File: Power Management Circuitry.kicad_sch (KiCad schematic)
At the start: 24 parts, among them J1 Barrel_Jack_Switch, Q1 IRF7309IPBF, SW2 SW_SPST, U2 AMS1117-3.3, U3 AMS1117-5.0, U4 LM358, U5 LM358

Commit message: Update Power Management Circuitry.kicad_sch
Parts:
- removed U4, U5: LM358, Package_SO:SO-8_3.9x4.9mm_P1.27mm, symbol Amplifier_Operational:LM358
- added R3: 10 kΩ, Resistor_SMD:R_1206_3216Metric_Pad1.30x1.75mm_HandSolder, symbol Device:R
- added U4: LM324, symbol Amplifier_Operational:LM324
- added U5: LM339, symbol Comparator:LM339
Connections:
- net +3V3: now also U5.4 (-)
- net +5V_{OCP}: now also R3.2, U5.3 (V+)
- net +V_{In}: now also U4.4 (V+)
- net -V_{In}: now also U4.11 (V-), U5.12 (V-)
- net at RV3.2: now also U4.10 (+)
- net at Q1.4 (G): now also R3.1, U5.2
- net at R3.2, R4.1: now also U4.6 (-)
- net at R4.2: now also U4.7, U4.9 (-)
- net at R3.1, R4.2: now also U5.5 (+)
- net at Q1.2 (G): now also U4.8
- net at RV2.2: now also U4.3 (+)
- net at RV1.2: now also U4.2 (-)
- net at RV1.3: now also U4.1, U4.5 (+)

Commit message: Schematic Revision C2
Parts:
- removed Q1: IRF7309IPBF, Package_SO:SOIC-8_3.9x4.9mm_P1.27mm, symbol Transistor_FET:IRF7309IPBF
- added Q1: AO3401A, Package_TO_SOT_SMD:SOT-23_Handsoldering, symbol Transistor_FET:AO3401A
- added Q2: SI2302, Package_TO_SOT_SMD:SOT-23_Handsoldering, symbol M's Library:SI2302
- D1: Local Seller https://microohm-eg.com/product/blue-led-5mm/ -> https://makerselectronics.com/product/blue-led-5mm-transpar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
- F1: footprint Fuse:Fuseholder_Clip-5x20mm_Littelfuse_520_Inline_P20.50x5.80mm_D1.30mm_Horizontal -> Fuse:Fuseholder_Cylinder-5x20mm_Schurter_0031_8201_Horizontal_Open; Local Seller https://makerselectronics.com/product/fuse-holder-on-pcb-fo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 -> https://makerselectronics.com/product/fuse-holder-5mm-x-20m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
- R2: Local Seller https://makerselectronics.com/product/chip-resistor-smd-330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 -> 0.22
- U4: footprint (none) -> Package_SO:SO-14_3.9x8.65mm_P1.27mm; Local Seller (none) -> https://makerselectronics.com/product/lm324-sop-14-operatio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
- U5: footprint (none) -> Package_SO:SOIC-14_3.9x8.7mm_P1.27mm; Local Seller (none) -> https://makerselectronics.com/product/lm339d-5mv-0-25ua-4-s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
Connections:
- net +5V: now also Q1.2 (S)
- net -V_{In}: now also Q2.2 (S)
- net GND: now also Q2.3 (D)
- net VBUS: now also Q1.3 (D)
- net at R3.1, U5.2: now also Q1.1 (G)
- net at U4.8: now also Q2.1 (G)
- no-connect marks 0 -> 2
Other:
- added sheet Unplaced Units (Unplaced Units.kicad_sch)

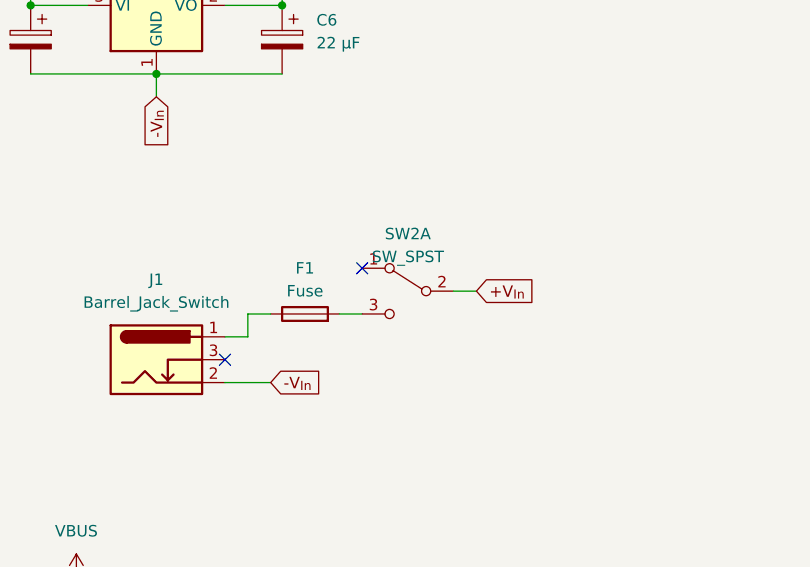
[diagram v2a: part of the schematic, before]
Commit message: Finished recreating the schematic
Created new footprints for DC Barrel Jack and Fuse Holder (3d models still require adjustment and finalize shunt resistance value and footprint)
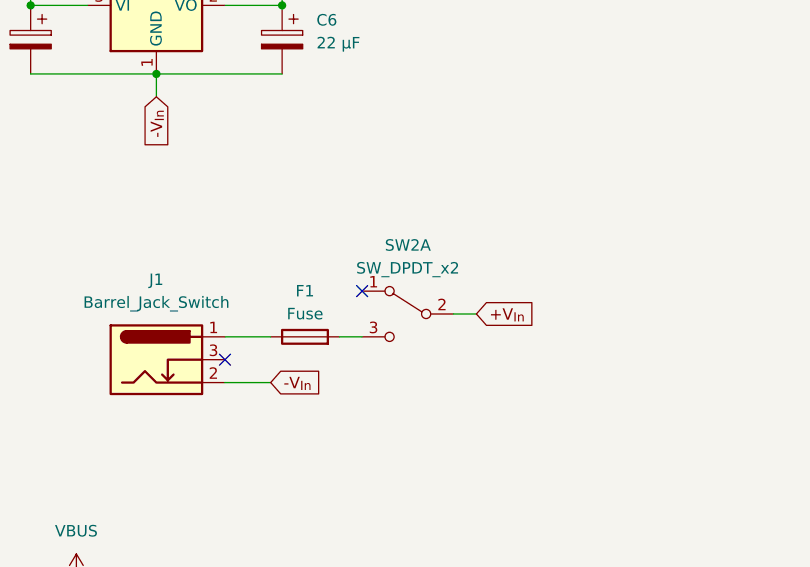
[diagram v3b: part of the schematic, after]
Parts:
- F1: footprint Fuse:Fuseholder_Cylinder-5x20mm_Schurter_0031_8201_Horizontal_Open -> M's Library:Fuseholder_with_Cover_5x20mm_Horizontal
- J1: footprint Connector_BarrelJack:BarrelJack_Horizontal -> M's Library:BarrelJack_Horizontal
- SW2: value SW_SPST -> SW_DPDT_x2; Local Seller https://microohm-eg.com/product/on-off-switch-6-pin-8x8mm/ -> https://makerselectronics.com/product/push-button-6-pins-se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
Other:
- moved on the sheet: F1
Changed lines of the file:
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@@
   (junction (at 38.1 71.12) (diameter 0) (color 0 0 0 0)
   )
-  (no_connect (at 74.93 100.33))
+  (no_connect (at 74.93 102.87))
   (no_connect (at 59.69 110.49))
-  (wire (pts (xy 62.23 105.41) (xy 62.23 107.95))
-    (stroke (width 0) (type default))
-  )
   (wire (pts (xy 208.28 74.93) (xy 207.01 74.93))
     (stroke (width 0) (type default))
@@
     (stroke (width 0) (type default))
   )
-  (wire (pts (xy 72.39 105.41) (xy 74.93 105.41))
+  (wire (pts (xy 72.39 107.95) (xy 74.93 107.95))
     (stroke (width 0) (type default))
   )
@@
     (stroke (width 0) (type default))
   )
-  (wire (pts (xy 62.23 105.41) (xy 64.77 105.41))
-    (stroke (width 0) (type default))
-  )
   (wire (pts (xy 254 144.78) (xy 254 147.32))
     (stroke (width 0) (type default))
@@
     (stroke (width 0) (type default))
   )
-  (wire (pts (xy 62.23 107.95) (xy 59.69 107.95))
+  (wire (pts (xy 59.69 107.95) (xy 64.77 107.95))
     (stroke (width 0) (type default))
   )
@@
     (stroke (width 0) (type default))
   )
-  (wire (pts (xy 85.09 102.87) (xy 87.63 102.87))
+  (wire (pts (xy 85.09 105.41) (xy 87.63 105.41))
     (stroke (width 0) (type default))
   )
@@
     )
   )
-  (global_label "+V_{In}" (shape input) (at 87.63 102.87 0) (fields_autoplaced)
+  (global_label "+V_{In}" (shape input) (at 87.63 105.41 0) (fields_autoplaced)
     (effects (font (size 1.27 1.27)) (justify left))
-    (property "Intersheetrefs" "${INTERSHEET_REFS}" (at 94.73 102.87 0)
+    (property "Intersheetrefs" "${INTERSHEET_REFS}" (at 94.73 105.41 0)
       (effects (font (size 1.27 1.27)) (justify left) hide)
     )
@@
     )
   )
-  (symbol (lib_id "Device:Fuse") (at 68.58 105.41 90) (unit 1)
+  (symbol (lib_id "Device:Fuse") (at 68.58 107.95 90) (unit 1)
     (in_bom yes) (on_board yes) (dnp no)
-    (property "Reference" "F1" (at 68.58 100.33 90)
-      (effects (font (size 1.27 1.27)))
-    )
-    (property "Value" "Fuse" (at 68.58 102.87 90)
-      (effects (font (size 1.27 1.27)))
-    )
-    (property "Footprint" "Fuse:Fuseholder_Cylinder-5x20mm_Schurter_0031_8201_Horizontal_Open" (at 68.58 107.188 90)
-      (effects (font (size 1.27 1.27)) hide)
-    )
-    (property "Datasheet" "~" (at 68.58 105.41 0)
-      (effects (font (size 1.27 1.27)) hide)
-    )
-    (property "Local Seller" "https://makerselectronics.com/product/fuse-holder-5mm-x-20mm-pcb-mount-blx-a" (at 68.58 105.41 0)
+    (property "Reference" "F1" (at 68.58 102.87 90)
+      (effects (font (size 1.27 1.27)))
+    )
+    (property "Value" "Fuse" (at 68.58 105.41 90)
+      (effects (font (size 1.27 1.27)))
+    )
+    (property "Footprint" "M's Library:Fuseholder_with_Cover_5x20mm_Horizontal" (at 68.58 109.728 90)
+      (effects (font (size 1.27 1.27)) hide)
+    )
+    (property "Datasheet" "~" (at 68.58 107.95 0)
+      (effects (font (size 1.27 1.27)) hide)
+    )
+    (property "Local Seller" "https://makerselectronics.com/product/fuse-holder-5mm-x-20mm-pcb-mount-blx-a" (at 68.58 107.95 0)
       (effects (font (size 1.27 1.27)) hide)
     )
@@
         (path "/bd689b4b-40d7-46ba-91b6-965ce30f8212/9da448d2-dd3c-46c7-b716-b331cd5a4621"
           (reference "F1") (unit 1)
-        )
-      )
-    )
-  )
-  (symbol (lib_id "Switch:SW_DPDT_x2") (at 80.01 102.87 0) (mirror y) (unit 1)
-    (in_bom yes) (on_board yes) (dnp no)
-    (property "Reference" "SW2" (at 80.01 96.52 0)
-      (effects (font (size 1.27 1.27)))
-    )
-    (property "Value" "SW_SPST" (at 80.01 99.06 0)
-      (effects (font (size 1.27 1.27)))
-    )
-    (property "Footprint" "Button_Switch_THT:SW_Push_2P2T_Toggle_CK_PVA2xxH1xxxxxxV2" (at 80.01 102.87 0)
-      (effects (font (size 1.27 1.27)) hide)
-    )
-    (property "Datasheet" "~" (at 80.01 102.87 0)
-      (effects (font (size 1.27 1.27)) hide)
-    )
-    (property "Local Seller" "https://microohm-eg.com/product/on-off-switch-6-pin-8x8mm/" (at 80.01 102.87 0)
-      (effects (font (size 1.27 1.27)) hide)
-    )
-    (pin "1")
-    (pin "2")
-    (pin "3")
-    (pin "4")
-    (pin "5")
-    (pin "6")
-    (instances
-      (project "[EXOTIC] AVR Kit"
-        (path "/bd689b4b-40d7-46ba-91b6-965ce30f8212/9da448d2-dd3c-46c7-b716-b331cd5a4621"
-          (reference "SW2") (unit 1)
         )
       )
@@
     )
   )
+  (symbol (lib_id "Switch:SW_DPDT_x2") (at 80.01 105.41 0) (mirror y) (unit 1)
+    (in_bom yes) (on_board yes) (dnp no) (fields_autoplaced)
+    (property "Reference" "SW2" (at 80.01 97.79 0)
+      (effects (font (size 1.27 1.27)))
+    )
+    (property "Value" "SW_DPDT_x2" (at 80.01 100.33 0)
+      (effects (font (size 1.27 1.27)))
+    )
+    (property "Footprint" "Button_Switch_THT:SW_Push_2P2T_Toggle_CK_PVA2xxH1xxxxxxV2" (at 80.01 105.41 0)
+      (effects (font (size 1.27 1.27)) hide)
+    )
+    (property "Datasheet" "~" (at 80.01 105.41 0)
+      (effects (font (size 1.27 1.27)) hide)
+    )
+    (property "Local Seller" "https://makerselectronics.com/product/push-button-6-pins-self-lock-8x8mm" (at 80.01 105.41 0)
+      (effects (font (size 1.27 1.27)) hide)
+    )
+    (pin "1")
+    (pin "2")
+    (pin "3")
+    (pin "4")
+    (pin "5")
+    (pin "6")
+    (instances
+      (project "[EXOTIC] AVR Kit"
+        (path "/bd689b4b-40d7-46ba-91b6-965ce30f8212/9da448d2-dd3c-46c7-b716-b331cd5a4621"
+          (reference "SW2") (unit 1)
+        )
+      )
+    )
+  )
   (symbol (lib_id "power:VBUS") (at 43.18 134.62 0) (unit 1)
     (in_bom yes) (on_board yes) (dnp no) (fields_autoplaced)
@@
       (effects (font (size 1.27 1.27)))
     )
-    (property "Footprint" "Connector_BarrelJack:BarrelJack_Horizontal" (at 53.34 111.506 0)
-      (effects (font (size 1.27 1.27)) hide)
-    )
+    (property "Footprint" "M's Library:BarrelJack_Horizontal" (at 53.34 111.506 0)
+      (effects (font (size 1.27 1.27)) hide)
+    )

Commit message: WIP2
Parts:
- removed C10: 100 nF, Capacitor_SMD:C_1206_3216Metric_Pad1.33x1.80mm_HandSolder, symbol Device:C
- removed C5: 10 µF, Capacitor_SMD:C_1206_3216Metric_Pad1.33x1.80mm_HandSolder, symbol Device:C_Polarized
- removed R2: 100 mΩ, Resistor_THT:R_Axial_DIN0414_L11.9mm_D4.5mm_P20.32mm_Horizontal, symbol Device:R
- removed R3: 6k8 Ω, Resistor_SMD:R_1206_3216Metric_Pad1.30x1.75mm_HandSolder, symbol Device:R
- removed SW2: SW_DPDT_x2, Button_Switch_THT:SW_Push_2P2T_Toggle_CK_PVA2xxH1xxxxxxV2, symbol Switch:SW_DPDT_x2
- removed unit 3 of U4
- removed unit 1 of U5
- added R4: 10 kΩ, Resistor_SMD:R_1206_3216Metric_Pad1.30x1.75mm_HandSolder, symbol Device:R
- added SW2: SW_DPDT_x2, Button_Switch_THT:SW_Push_2P2T_Toggle_CK_PVA2xxH1xxxxxxV2, symbol Switch:SW_DPDT_x2
- added unit 4 of U4
- added unit 4 of U5
- R4: value 10 kΩ -> 6.8 kΩ
- renumbered R7 to R6
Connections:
- net +3V3: now also U5.8 (-)
- net +5V: now also C5.1, R3.2, RV1.3, U2.3 (VI), U5.3 (V+); no longer RV1.1
- net +5V_{OCP}: now also RV2.3; no longer C5.1, R3.2, RV2.1, U2.3 (VI), U5.3 (V+)
- net +V_{In}: now also F1.2, R4.2
- net -V_{In}: now also RV2.1; no longer R4.1, RV2.3, U5.12 (V-)
- net GND: now also R4.1, U5.12 (V-)
- net at RV3.2: now also U4.12 (+)
- net at U4.2 (-): now also R3.2, R4.1; no longer RV1.2
- net at U4.3 (+): now also RV1.1, U4.7; no longer RV2.2
- net at Q1.1 (G), R3.1: now also U5.14
- net at Q2.1 (G): now also U4.14
- net at R4.2: now also U4.1, U4.13 (-); no longer U4.7
- net at F1.1: now also SW2.5 (B); no longer J1.1
- net at R4.2: now also R4.1, U5.9 (+)
- new net: RV2.2, U4.5 (+)
- new net: RV1.2, U4.6 (-)
- new net: J1.1, SW2.6 (C)
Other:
- added sheet Shunt Resistor Array (Shunt Resistor Array.kicad_sch)
- note added: "To Do: ~Priority Switch to select which 5V source is the dominant~"
- note removed: "To Do: Priority Switch to select which 5V source is the dominant"
- moved on the sheet: F1, Q2, RV1, RV2, U4A, U4B

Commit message: Most work done
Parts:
- renumbered R6 to R7
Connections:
- net +5V_{OCP}: now also RV3.3; no longer RV3.1
- net -V_{In}: now also RV3.1; no longer RV3.3
- net at F1.1: now also SW2.6 (C); no longer SW2.5 (B)
- net at J1.1: now also SW2.5 (B); no longer SW2.6 (C)
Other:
- moved on the sheet: F1, RV3, SW2B
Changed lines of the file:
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@@
   (junction (at 38.1 71.12) (diameter 0) (color 0 0 0 0)
   )
-  (no_connect (at 63.5 102.87))
+  (no_connect (at 78.74 110.49))
   (no_connect (at 59.69 110.49))
   (wire (pts (xy 208.28 74.93) (xy 207.01 74.93))
@@
     (stroke (width 0) (type default))
   )
-  (wire (pts (xy 59.69 107.95) (xy 63.5 107.95))
-    (stroke (width 0) (type default))
-  )
   (wire (pts (xy 152.4 45.72) (xy 152.4 46.99))
     (stroke (width 0) (type default))
@@
     (stroke (width 0) (type default))
   )
+  (wire (pts (xy 59.69 107.95) (xy 68.58 107.95))
+    (stroke (width 0) (type default))
+  )
   (wire (pts (xy 38.1 40.64) (xy 44.45 40.64))
     (stroke (width 0) (type default))
@@
     (stroke (width 0) (type default))
   )
+  (wire (pts (xy 81.28 105.41) (xy 78.74 105.41))
+    (stroke (width 0) (type default))
+  )
   (wire (pts (xy 185.42 109.22) (xy 182.88 109.22))
     (stroke (width 0) (type default))
@@
     (stroke (width 0) (type default))
   )
-  (wire (pts (xy 83.82 105.41) (xy 86.36 105.41))
+  (wire (pts (xy 88.9 105.41) (xy 91.44 105.41))
     (stroke (width 0) (type default))
   )
@@
   )
   (wire (pts (xy 191.77 64.77) (xy 195.58 64.77))
-    (stroke (width 0) (type default))
-  )
-  (wire (pts (xy 73.66 105.41) (xy 76.2 105.41))
     (stroke (width 0) (type default))
   )
@@
     )
   )
-  (global_label "+V_{In}" (shape input) (at 86.36 105.41 0) (fields_autoplaced)
+  (global_label "+V_{In}" (shape input) (at 91.44 105.41 0) (fields_autoplaced)
     (effects (font (size 1.27 1.27)) (justify left))
-    (property "Intersheetrefs" "${INTERSHEET_REFS}" (at 93.46 105.41 0)
+    (property "Intersheetrefs" "${INTERSHEET_REFS}" (at 98.54 105.41 0)
       (effects (font (size 1.27 1.27)) (justify left) hide)
     )
@@
     )
   )
-  (symbol (lib_id "Device:R_Potentiometer") (at 215.9 29.21 90) (mirror x) (unit 1)
+  (symbol (lib_id "Device:R_Potentiometer") (at 215.9 29.21 270) (unit 1)
     (in_bom yes) (on_board yes) (dnp no)
     (property "Reference" "RV3" (at 215.9 22.86 90)
@@
     )
   )
-  (symbol (lib_id "Device:Fuse") (at 80.01 105.41 90) (unit 1)
+  (symbol (lib_id "Device:Fuse") (at 85.09 105.41 90) (unit 1)
     (in_bom yes) (on_board yes) (dnp no)
-    (property "Reference" "F1" (at 80.01 100.33 90)
-      (effects (font (size 1.27 1.27)))
-    )
-    (property "Value" "Fuse" (at 80.01 102.87 90)
-      (effects (font (size 1.27 1.27)))
-    )
-    (property "Footprint" "M's Library:Fuseholder_with_Cover_5x20mm_Horizontal" (at 80.01 107.188 90)
-      (effects (font (size 1.27 1.27)) hide)
-    )
-    (property "Datasheet" "~" (at 80.01 105.41 0)
-      (effects (font (size 1.27 1.27)) hide)
-    )
-    (property "Local Seller" "https://makerselectronics.com/product/fuse-holder-5mm-x-20mm-pcb-mount-blx-a" (at 80.01 105.41 0)
+    (property "Reference" "F1" (at 85.09 100.33 90)
+      (effects (font (size 1.27 1.27)))
+    )
+    (property "Value" "Fuse" (at 85.09 102.87 90)
+      (effects (font (size 1.27 1.27)))
+    )
+    (property "Footprint" "M's Library:Fuseholder_with_Cover_5x20mm_Horizontal" (at 85.09 107.188 90)
+      (effects (font (size 1.27 1.27)) hide)
+    )
+    (property "Datasheet" "~" (at 85.09 105.41 0)
+      (effects (font (size 1.27 1.27)) hide)
+    )
+    (property "Local Seller" "https://makerselectronics.com/product/fuse-holder-5mm-x-20mm-pcb-mount-blx-a" (at 85.09 105.41 0)
       (effects (font (size 1.27 1.27)) hide)
     )
@@
   (symbol (lib_id "Device:R") (at 168.91 151.13 90) (unit 1)
     (in_bom yes) (on_board yes) (dnp no) (fields_autoplaced)
-    (property "Reference" "R6" (at 168.91 144.78 90)
+    (property "Reference" "R7" (at 168.91 144.78 90)
       (effects (font (size 1.27 1.27)))
     )
@@
       (project "[EXOTIC] AVR Kit"
         (path "/bd689b4b-40d7-46ba-91b6-965ce30f8212/9da448d2-dd3c-46c7-b716-b331cd5a4621"
-          (reference "R6") (unit 1)
+          (reference "R7") (unit 1)
         )
       )
@@
         )
         (path "/bd689b4b-40d7-46ba-91b6-965ce30f8212/9da448d2-dd3c-46c7-b716-b331cd5a4621"
-          (reference "R5") (unit 1)
+          (reference "R6") (unit 1)
         )
       )
@@
     )
   )
-  (symbol (lib_id "Switch:SW_DPDT_x2") (at 68.58 105.41 0) (mirror y) (unit 2)
-    (in_bom yes) (on_board yes) (dnp no) (fields_autoplaced)
-    (property "Reference" "SW2" (at 68.58 97.79 0)
-      (effects (font (size 1.27 1.27)))
-    )
-    (property "Value" "SW_DPDT_x2" (at 68.58 100.33 0)
-      (effects (font (size 1.27 1.27)))
-    )
-    (property "Footprint" "Button_Switch_THT:SW_Push_2P2T_Toggle_CK_PVA2xxH1xxxxxxV2" (at 68.58 105.41 0)
-      (effects (font (size 1.27 1.27)) hide)
-    )
-    (property "Datasheet" "~" (at 68.58 105.41 0)
-      (effects (font (size 1.27 1.27)) hide)
-    )
-    (property "Local Seller" "https://makerselectronics.com/product/push-button-6-pins-self-lock-8x8mm" (at 68.58 105.41 0)
+  (symbol (lib_id "Switch:SW_DPDT_x2") (at 73.66 107.95 0) (mirror x) (unit 2)
+    (in_bom yes) (on_board yes) (dnp no) (fields_autoplaced)
+    (property "Reference" "SW2" (at 73.66 100.33 0)
+      (effects (font (size 1.27 1.27)))
+    )
+    (property "Value" "SW_DPDT_x2" (at 73.66 102.87 0)
+      (effects (font (size 1.27 1.27)))
+    )
+    (property "Footprint" "Button_Switch_THT:SW_Push_2P2T_Toggle_CK_PVA2xxH1xxxxxxV2" (at 73.66 107.95 0)
+      (effects (font (size 1.27 1.27)) hide)
+    )
+    (property "Datasheet" "~" (at 73.66 107.95 0)
+      (effects (font (size 1.27 1.27)) hide)
+    )
+    (property "Local Seller" "https://makerselectronics.com/product/push-button-6-pins-self-lock-8x8mm" (at 73.66 107.95 0)
       (effects (font (size 1.27 1.27)) hide)
     )
@@
         )
         (path "/bd689b4b-40d7-46ba-91b6-965ce30f8212/9da448d2-dd3c-46c7-b716-b331cd5a4621"
-          (reference "R4") (unit 1)
+          (reference "R5") (unit 1)
         )
       )
@@
         )
         (path "/bd689b4b-40d7-46ba-91b6-965ce30f8212/9da448d2-dd3c-46c7-b716-b331cd5a4621"
-          (reference "R17") (unit 1)
-        )
-      )
+          (reference "R4") (unit 1)
+        )
+      )

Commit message: done something
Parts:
- SW2: footprint Button_Switch_THT:SW_Push_2P2T_Toggle_CK_PVA2xxH1xxxxxxV2 -> M's Library:SW_Push_DPDT_Toggle_7.0mm
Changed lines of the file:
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@@
       (effects (font (size 1.27 1.27)))
     )
-    (property "Footprint" "Button_Switch_THT:SW_Push_2P2T_Toggle_CK_PVA2xxH1xxxxxxV2" (at 73.66 107.95 0)
+    (property "Footprint" "M's Library:SW_Push_DPDT_Toggle_7.0mm" (at 73.66 107.95 0)
       (effects (font (size 1.27 1.27)) hide)
     )
